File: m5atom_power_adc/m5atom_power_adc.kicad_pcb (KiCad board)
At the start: 2 copper layers, 0 parts

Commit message: refactor: 回路図をフラットから階層化に移行、ブザー回路追加
- 回路図: フラット構成から階層シート構成へ移行（共通回路の共通化）
  - メインシート（1xx）: 電源・ESP32・ADC・ブザー等トップレベル
  - RelayControl サブシート: リレードライバ回路（Q×2、D×3、R×6）
  - VoltageSense サブシート: 電圧分圧回路（C×4、R×5）
  - GroveUnit サブシート: Grove 電源スイッチ回路（Q×3、D×3、R×3）
- 回路図: リファレンス番号をページ番号+xx体系に変更
- 回路図: ブザー回路追加（LS101/MLT-8530 + Q103/AO3401A ハイサイドスイッチ、GPIO34）
- HARDWARE.md: ブザー回路仕様を追記（駆動条件・部品表）
- HARDWARE.md: 赤色LED選定（XL-1608SURC-06）追記
- HARDWARE.md: 電源系統別トレース幅・ビアサイズ表を拡充
- HARDWARE.md: LM2596スイッチングノードの配線注意事項を追記

Co-Authored-By: Claude Sonnet 4.6 <noreply@anthropic.com>
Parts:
- added C101: 220uF, Capacitor_SMD:CP_Elec_10x10, F.Cu at (33.8, 158.8)
- added C102: 220uF, Capacitor_SMD:CP_Elec_10x10, F.Cu at (56.6, 144.9)
- added C103: 10uF, Capacitor_SMD:C_0805_2012Metric, F.Cu at (116.4, 105.7)
- added C104: 1uF X7R, Capacitor_SMD:C_0603_1608Metric, F.Cu at (126.8, 109.6)
- added C105: 10uF, Capacitor_SMD:C_0805_2012Metric, F.Cu at (116.4, 108.7)
- added C106: 100nF C0G, Capacitor_SMD:C_1206_3216Metric, F.Cu at (94.2, 108.4)
- added C107: 100nF C0G, Capacitor_SMD:C_1206_3216Metric, F.Cu at (94.2, 121.8)
- added C108: 10uF, Capacitor_SMD:C_0805_2012Metric, F.Cu at (116.4, 111.7)
- added C109: 10uF, Capacitor_SMD:C_0805_2012Metric, F.Cu at (116.4, 114.7)
- added C110: 100nF C0G, Capacitor_SMD:C_1206_3216Metric, F.Cu at (94.2, 111.7)
- added C701: 22nF C0G, Capacitor_SMD:C_0805_2012Metric, F.Cu at (230.7, 135.1)
- added C702: 22nF C0G, Capacitor_SMD:C_0805_2012Metric, F.Cu at (230.7, 129.2)
- added C703: 220nF C0G, Capacitor_SMD:C_1206_3216Metric, F.Cu at (233.0, 132.2)
- added C801: 22nF C0G, Capacitor_SMD:C_0805_2012Metric, F.Cu at (243.9, 135.4)
- added C802: 22nF C0G, Capacitor_SMD:C_0805_2012Metric, F.Cu at (238.0, 135.4)
- added C803: 220nF C0G, Capacitor_SMD:C_1206_3216Metric, F.Cu at (241.0, 133.1)
- added D101: SMAJ16A, Diode_SMD:D_SMB, F.Cu at (32.4, 148.8)
- added D102: SSL36, Diode_SMD:D_SMA, F.Cu at (36.7, 148.6)
- added D103: LESD5D5.0CT1G, Diode_SMD:D_SOD-523, F.Cu at (98.8, 112.6)
- added D104: LESD5D5.0CT1G, Diode_SMD:D_SOD-523, F.Cu at (98.8, 115.0)
- added D105: SSL36, Diode_SMD:D_SMA, F.Cu at (81.3, 118.0)
- added D106: LESD5D5.0CT1G, Diode_SMD:D_SOD-523, F.Cu at (98.8, 117.5)
- added D107: SS34, Diode_SMD:D_SMA, F.Cu at (43.1, 157.0)
- added D108: LED, LED_SMD:LED_0603_1608Metric, F.Cu at (52.3, 161.3)
- added D109: 1N4148WS, Diode_SMD:D_SOD-323, F.Cu at (120.8, 126.3)
- added D201: 1N4148WS, Diode_SMD:D_SOD-323, F.Cu at (112.3, 151.8)
- added D202: LED, LED_SMD:LED_0603_1608Metric, F.Cu at (117.8, 157.3)
- added D301: 1N4148WS, Diode_SMD:D_SOD-323, F.Cu at (128.0, 151.8)
- added D302: LED, LED_SMD:LED_0603_1608Metric, F.Cu at (133.5, 157.3)
- added D401: 1N4148WS, Diode_SMD:D_SOD-323, F.Cu at (143.7, 151.8)
- added D402: LED, LED_SMD:LED_0603_1608Metric, F.Cu at (149.2, 157.3)
- added D501: SD03, Diode_SMD:D_SOD-323, F.Cu at (250.4, 52.1)
- added D502: SD03, Diode_SMD:D_SOD-323, F.Cu at (250.4, 55.1)
- added D601: SD03, Diode_SMD:D_SOD-323, F.Cu at (257.2, 86.1)
- added D602: SD03, Diode_SMD:D_SOD-323, F.Cu at (257.2, 89.0)
- added F101: Polyfuse, Fuse:Fuse_1812_4532Metric, F.Cu at (36.7, 141.8)
- added FB101: 500mA 600Ω@100MHz, Inductor_SMD:L_0805_2012Metric, F.Cu at (99.3, 124.6)
- added J101: USB_C_Receptacle_USB2.0_16P, Connector_USB:USB_C_Receptacle_HRO_TYPE-C-31-M-12, F.Cu at (54.0, 96.5)
- added J102: Conn_01x04_Pin, Connector_PinHeader_2.54mm:PinHeader_1x04_P2.54mm_Vertical, F.Cu at (143.1, 72.3)
- added J103: SubBatt, Connector_JST:JST_XH_B2B-XH-A_1x02_P2.50mm_Vertical, F.Cu at (54.0, 65.5)
- added J104: MainBatt, Connector_JST:JST_XH_B2B-XH-A_1x02_P2.50mm_Vertical, F.Cu at (54.0, 56.2)
- added J105: I2C, Connector_JST:JST_XH_S4B-XH-SM4-TB_1x04-1MP_P2.50mm_Horizontal, F.Cu at (58.3, 122.2)
- added J106: Shunt, Connector_JST:JST_XH_B2B-XH-A_1x02_P2.50mm_Vertical, F.Cu at (150.0, 59.5)
- added J201: Relay0, Connector_JST:JST_XH_B2B-XH-A_1x02_P2.50mm_Vertical, F.Cu at (113.7, 156.8)
- added J202: R0SW, Connector_JST:JST_XH_B2B-XH-A_1x02_P2.50mm_Vertical, F.Cu at (113.7, 169.2)
- added J301: Relay0, Connector_JST:JST_XH_B2B-XH-A_1x02_P2.50mm_Vertical, F.Cu at (129.3, 156.8)
- added J302: R0SW, Connector_JST:JST_XH_B2B-XH-A_1x02_P2.50mm_Vertical, F.Cu at (129.3, 169.2)
- added J401: Relay0, Connector_JST:JST_XH_B2B-XH-A_1x02_P2.50mm_Vertical, F.Cu at (145.1, 156.8)
- added J402: R0SW, Connector_JST:JST_XH_B2B-XH-A_1x02_P2.50mm_Vertical, F.Cu at (145.1, 169.2)
- added J501: GROVE-CONNECTOR, 000_Local:HY2.0-4PWB, F.Cu at (251.2, 46.7)
- added J601: GROVE-CONNECTOR, 000_Local:HY2.0-4PWB, F.Cu at (257.9, 80.7)
- added L101: 68uH, 000_Local:PSPMAA0605H-680M-IGF, F.Cu at (54.1, 156.3)
- added LS101: MLT-8530, 000_Local:MLT-8530, F.Cu at (65.5, 105.0)
- added Q101: AO3401A, Package_TO_SOT_SMD:SOT-23, F.Cu at (111.7, 94.0)
- added Q102: MMBT2222A, Package_TO_SOT_SMD:SOT-23, F.Cu at (111.7, 98.5)
- added Q103: AO3401A, Package_TO_SOT_SMD:SOT-23, F.Cu at (111.7, 102.9)
- added Q201: MMBT2222A, Package_TO_SOT_SMD:SOT-23, F.Cu at (111.8, 161.7)
- added Q301: MMBT2222A, Package_TO_SOT_SMD:SOT-23, F.Cu at (127.5, 161.7)
- added Q401: MMBT2222A, Package_TO_SOT_SMD:SOT-23, F.Cu at (143.2, 161.7)
- added Q501: AO3401A, Package_TO_SOT_SMD:SOT-23, F.Cu at (260.1, 41.0)
- added Q502: MMBT2222A, Package_TO_SOT_SMD:SOT-23, F.Cu at (260.1, 45.4)
- added Q601: AO3401A, Package_TO_SOT_SMD:SOT-23, F.Cu at (266.9, 74.9)
- added Q602: MMBT2222A, Package_TO_SOT_SMD:SOT-23, F.Cu at (266.9, 79.4)
- added R101: 10k, Resistor_SMD:R_0402_1005Metric, F.Cu at (51.5, 151.5)
- added R102: 5.1k, Resistor_SMD:R_0603_1608Metric, F.Cu at (126.8, 112.1)
- added R103: 5.1k, Resistor_SMD:R_0603_1608Metric, F.Cu at (126.8, 114.6)
- added R104: 1k, Resistor_SMD:R_0603_1608Metric, F.Cu at (55.6, 161.3)
- added R105: 10k, Resistor_SMD:R_0402_1005Metric, F.Cu at (125.2, 71.0)
- added R106: 100k, Resistor_SMD:R_0603_1608Metric, F.Cu at (134.8, 124.6)
- added R107: 2W4.7, Resistor_SMD:R_2512_6332Metric, F.Cu at (108.7, 107.6)
- added R108: 2W4.7, Resistor_SMD:R_2512_6332Metric, F.Cu at (108.7, 112.5)
- added R109: 2W4.7, Resistor_SMD:R_2512_6332Metric, F.Cu at (108.7, 117.4)
- added R110: 10k, Resistor_SMD:R_0402_1005Metric, F.Cu at (131.0, 73.0)
- added R111: 10k, Resistor_SMD:R_0402_1005Metric, F.Cu at (131.0, 75.0)
- added R112: 10k, Resistor_SMD:R_0402_1005Metric, F.Cu at (128.1, 77.0)
- added R113: 10k, Resistor_SMD:R_0402_1005Metric, F.Cu at (125.2, 75.0)
- added R114: 10k, Resistor_SMD:R_0402_1005Metric, F.Cu at (125.2, 77.0)
- added R201: 100k, Resistor_SMD:R_0603_1608Metric, F.Cu at (114.0, 173.1)
- added R202: 27k, Resistor_SMD:R_0603_1608Metric, F.Cu at (110.9, 173.1)
- added R203: 1k, Resistor_SMD:R_0603_1608Metric, F.Cu at (116.2, 151.6)
- added R204: 1k, Resistor_SMD:R_0603_1608Metric, F.Cu at (117.8, 154.2)
- added R205: 1k, Resistor_SMD:R_0603_1608Metric, F.Cu at (108.9, 162.1)
- added R301: 100k, Resistor_SMD:R_0603_1608Metric, F.Cu at (129.7, 173.1)
- added R302: 27k, Resistor_SMD:R_0603_1608Metric, F.Cu at (126.6, 173.1)
- added R303: 1k, Resistor_SMD:R_0603_1608Metric, F.Cu at (131.9, 151.6)
- added R304: 1k, Resistor_SMD:R_0603_1608Metric, F.Cu at (133.5, 154.2)
- added R305: 1k, Resistor_SMD:R_0603_1608Metric, F.Cu at (124.6, 162.1)
- added R401: 100k, Resistor_SMD:R_0603_1608Metric, F.Cu at (145.4, 173.1)
- added R402: 27k, Resistor_SMD:R_0603_1608Metric, F.Cu at (142.3, 173.1)
- added R403: 1k, Resistor_SMD:R_0603_1608Metric, F.Cu at (147.6, 151.6)
- added R404: 1k, Resistor_SMD:R_0603_1608Metric, F.Cu at (149.2, 154.2)
- added R405: 1k, Resistor_SMD:R_0603_1608Metric, F.Cu at (140.3, 162.1)
- added R501: 100k, Resistor_SMD:R_0603_1608Metric, F.Cu at (254.5, 51.9)
- added R502: 10k, Resistor_SMD:R_0402_1005Metric, F.Cu at (254.0, 54.1)
- added R601: 100k, Resistor_SMD:R_0603_1608Metric, F.Cu at (261.3, 85.8)
- added R602: 10k, Resistor_SMD:R_0402_1005Metric, F.Cu at (260.7, 88.1)
- added R701: 680k, Resistor_SMD:R_0603_1608Metric, F.Cu at (228.8, 130.8)
- added R702: 22k, Resistor_SMD:R_0402_1005Metric, F.Cu at (229.1, 133.4)
- added R703: 100, Resistor_SMD:R_0402_1005Metric, F.Cu at (230.8, 131.6)
- added R704: 100, Resistor_SMD:R_0402_1005Metric, F.Cu at (230.8, 132.8)
- added R801: 680k, Resistor_SMD:R_0603_1608Metric, F.Cu at (239.6, 137.3)
- added R802: 22k, Resistor_SMD:R_0402_1005Metric, F.Cu at (242.2, 137.0)
- added R803: 100, Resistor_SMD:R_0402_1005Metric, F.Cu at (240.4, 135.3)
- added R804: 100, Resistor_SMD:R_0402_1005Metric, F.Cu at (241.6, 135.3)
- added SW101: Boot, Button_Switch_SMD:SW_SPST_PTS810, F.Cu at (150.1, 110.7)
- added SW102: Reset, Button_Switch_SMD:SW_SPST_PTS810, F.Cu at (150.1, 115.4)
- added SW103: ~, Button_Switch_SMD:SW_SPST_PTS810, F.Cu at (150.1, 120.2)
- added SW104: ~, Button_Switch_SMD:SW_SPST_PTS810, F.Cu at (150.1, 124.9)
- added TP101: TestPoint, TestPoint:TestPoint_Pad_D1.5mm, F.Cu at (115.9, 84.7)
- added TP102: TestPoint, TestPoint:TestPoint_Pad_D1.5mm, F.Cu at (119.5, 91.8)
- added TP103: TestPoint, TestPoint:TestPoint_Pad_D1.5mm, F.Cu at (115.9, 88.2)
- added TP104: TestPoint, TestPoint:TestPoint_Pad_D1.5mm, F.Cu at (123.0, 98.9)
- added TP105: TestPoint, TestPoint:TestPoint_Pad_D1.5mm, F.Cu at (123.0, 102.4)
- added TP106: TestPoint, TestPoint:TestPoint_Pad_D1.5mm, F.Cu at (115.9, 102.4)
- added TP107: TestPoint, TestPoint:TestPoint_Pad_D1.5mm, F.Cu at (115.9, 91.8)
- added TP108: TestPoint, TestPoint:TestPoint_Pad_D1.5mm, F.Cu at (115.9, 98.9)
- added TP109: TestPoint, TestPoint:TestPoint_Pad_D1.5mm, F.Cu at (115.9, 95.3)
- added TP201: TestPoint, TestPoint:TestPoint_Pad_D1.5mm, F.Cu at (116.4, 161.4)
- added TP301: TestPoint, TestPoint:TestPoint_Pad_D1.5mm, F.Cu at (132.1, 161.4)
- added TP401: TestPoint, TestPoint:TestPoint_Pad_D1.5mm, F.Cu at (147.8, 161.4)
- added TP501: TestPoint, TestPoint:TestPoint_Pad_D1.5mm, F.Cu at (246.5, 52.4)
- added TP502: TestPoint, TestPoint:TestPoint_Pad_D1.5mm, F.Cu at (246.5, 56.0)
- added TP601: TestPoint, TestPoint:TestPoint_Pad_D1.5mm, F.Cu at (253.2, 86.4)
- added TP602: TestPoint, TestPoint:TestPoint_Pad_D1.5mm, F.Cu at (253.2, 89.9)
- added TP701: TestPoint, TestPoint:TestPoint_Pad_D1.5mm, F.Cu at (228.4, 127.9)
- added TP801: TestPoint, TestPoint:TestPoint_Pad_D1.5mm, F.Cu at (236.7, 137.7)
- added U101: LM2596S-5, Package_TO_SOT_SMD:TO-263-5_TabPin3, F.Cu at (44.7, 142.1)
- added U102: AMS1117-3.3, Package_TO_SOT_SMD:SOT-223-3_TabPin2, F.Cu at (83.0, 68.0)
- added U103: ESP32-S3-MINI-1, RF_Module:ESP32-S2-MINI-1, F.Cu at (105.5, 46.8)
- added U104: AMS1117-3.3, Package_TO_SOT_SMD:SOT-223-3_TabPin2, F.Cu at (174.3, 94.5)
- added U105: LTC2944, Package_DFN_QFN:DFN-8-1EP_3x3mm_P0.5mm_EP1.65x2.38mm, F.Cu at (174.1, 122.8)
- added U106: ADS1115IDGS, Package_SO:TSSOP-10_3x3mm_P0.5mm, F.Cu at (237.2, 130.0)
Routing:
- net +12V: track 0.00 -> 40.8 mm
- net GND1: track 0.00 -> 35.8 mm, vias 0 -> 14
- net GND2: track 0.00 -> 34.8 mm
- net Net-(D301-A): track 0.00 -> 32.6 mm
- net Net-(D201-A): track 0.00 -> 32.6 mm
- net Net-(D401-A): track 0.00 -> 32.6 mm
- net +5V: track 0.00 -> 25.4 mm
- net Net-(D107-K): track 0.00 -> 13.9 mm
- net /Relay2: track 0.00 -> 13.0 mm
- net /Relay1: track 0.00 -> 13.0 mm
- net /Relay0: track 0.00 -> 13.0 mm
- net /AIN2: track 0.00 -> 9.40 mm
- net /AIN0: track 0.00 -> 9.09 mm
- net /AIN3: track 0.00 -> 8.41 mm
- net /AIN1: track 0.00 -> 7.20 mm
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- added copper zone on B.Cu, net GND1

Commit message: fix: PCBレイアウトに合わせて回路図・PCBを微修正
Co-Authored-By: Claude Sonnet 4.6 <noreply@anthropic.com>
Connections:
- U103 pad 15: /Relay1 -> /RelaySense0
- U103 pad 16: /Relay2 -> /Relay1
- U103 pad 17: /RelaySense0 -> /RelaySense1
- U103 pad 18: /RelaySense1 -> /Relay2

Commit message: feat: PCBレイアウト完成・ドキュメントにサブシート構成を反映
- m5atom_power_adc: PCBレイアウト完成（80×82.5mm、131部品、ルーティング完了）
- GroveUnit/RelayControl サブシート更新
- CONTEXT.md/README.md: m5atom_power_adc のファイル構成にサブシート3枚・Library.pretty を追記

Co-Authored-By: Claude Sonnet 4.6 <noreply@anthropic.com>
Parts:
- removed R108, R109: 2W4.7, Resistor_SMD:R_2512_6332Metric
- removed TP106, TP108: TestPoint, TestPoint:TestPoint_Pad_D1.5mm
- added NT101: NetTie_2, NetTie:NetTie-2_SMD_Pad2.0mm, B.Cu at (74.8, 46.7)
- added NT102: NetTie_3_Tee, NetTie:NetTie-3_SMD_Pad2.0mm, B.Cu at (73.5, 90.0)
- added NT104: NetTie_2, NetTie:NetTie-2_SMD_Pad0.5mm, B.Cu at (119.0, 97.0)
- J301: value Relay0 -> Relay1
- J302: value R0SW -> R1SW
- J401: value Relay0 -> Relay2
- J402: value R0SW -> R2SW
- R107: value 2W4.7 -> 3W4.7
- SW103: value ~ -> Btn0
- SW104: value ~ -> Btn1
- moved Q601 196.8 mm to (72.3, 104.2), turned to -90 degrees
- moved D601 194.6 mm to (63.8, 107.8), turned to 180 degrees
- moved Q602 192.5 mm to (75.7, 102.1), turned to -90 degrees
- moved J601 191.5 mm to (69.4, 113.9)
- moved R601 189.6 mm to (72.3, 101.4)
- moved D602 188.2 mm to (69.6, 104.3), turned to 90 degrees
- moved R602 184.4 mm to (76.6, 99.1), turned to -90 degrees
- moved Q501 183.6 mm to (87.8, 104.2), turned to -90 degrees
- moved D501 180.0 mm to (79.3, 107.8), turned to 180 degrees
- moved J501 179.4 mm to (84.9, 113.9)
- moved TP601 178.8 mm to (75.8, 108.1)
- moved Q502 178.2 mm to (91.2, 102.1), turned to -90 degrees
- moved TP602 178.1 mm to (75.8, 105.4)
- moved R501 173.9 mm to (87.8, 101.4)
- moved D502 172.5 mm to (85.1, 104.3), turned to 90 degrees
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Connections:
- D501 pad 2: GND2 -> GND1
- D502 pad 2: GND2 -> GND1
- D601 pad 2: GND2 -> GND1
- D602 pad 2: GND2 -> GND1
- J102 pad 3: TXD0 -> RXD0
- J102 pad 4: RXD0 -> TXD0
- J103 pad 2: /BATT0_P -> +BATT
- J105 pad 1: GND2 -> GND1
- J202 pad 2: GND2 -> GND1
- J302 pad 2: GND2 -> GND1
- J402 pad 2: GND2 -> GND1
- J501 pad 4: GND2 -> GND1
- J601 pad 4: GND2 -> GND1
- Q102 pad 2: GND2 -> GND1
- Q201 pad 2: GND2 -> GND1
- Q301 pad 2: GND2 -> GND1
- Q401 pad 2: GND2 -> GND1
- Q502 pad 2: GND2 -> GND1
- Q602 pad 2: GND2 -> GND1
- R202 pad 2: GND2 -> GND1
- R302 pad 2: GND2 -> GND1
- R402 pad 2: GND2 -> GND1
- R701 pad 1: /BATT0_P -> /BATT1_P
- R702 pad 2: /BATT0_N -> /BATT1_N
- R704 pad 1: /BATT0_N -> /BATT1_N
- R801 pad 1: /BATT1_P -> +BATT
- R802 pad 2: /BATT1_N -> /BATT0_N
- R804 pad 1: /BATT1_N -> /BATT0_N
- U103 pad 10: /LTE_RX -> /LTE_EN
- U103 pad 14: /Relay0 -> /RelaySense0
- U103 pad 15: /RelaySense0 -> /Relay0
- U103 pad 16: /Relay1 -> /RelaySense1
- U103 pad 17: /RelaySense1 -> /Relay1
- U103 pad 18: /Relay2 -> /RelaySense2
- U103 pad 19: /RelaySense2 -> /Relay2
- U103 pad 20: /GU_EN -> /GU_0
- U103 pad 21: /GU_0 -> /GU_1
- U103 pad 22: /GU_1 -> /GU_EN
- U103 pad 8: /LTE_EN -> /LTE_RX
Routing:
- net +5V: track 25.4 -> 177.3 mm, vias 0 -> 7
- net +3.3V: track 0.00 -> 133.1 mm, vias 0 -> 5
- net SCL: track 0.00 -> 128.6 mm, vias 0 -> 4
- net SDA: track 0.00 -> 115.8 mm, vias 0 -> 4
- net /BATT0_N: track 0.00 -> 109.4 mm, vias 0 -> 3
- net +BATT: track 0.00 -> 99.1 mm, vias 0 -> 2
- net /BATT1_P: track 0.00 -> 82.8 mm, vias 0 -> 2
- net /BATT1_N: track 0.00 -> 82.6 mm, vias 0 -> 2
- net /LTE_RX: track 0.00 -> 80.3 mm
- net /LTE_TX: track 0.00 -> 78.3 mm
- net VBUS: track 3.37 -> 78.9 mm, vias 0 -> 2
- net /GU_0: track 0.00 -> 67.6 mm, vias 0 -> 2
- net GND2: track 34.8 -> 101.6 mm, vias 0 -> 23
- net /GU_1: track 0.00 -> 66.7 mm, vias 0 -> 2
- net ADC_RDY: track 0.00 -> 64.4 mm, vias 0 -> 2
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- added copper zone on B.Cu, net GND2
- added copper zone on B.Cu, net GNDA
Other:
- board outline added: 80 x 82.5 mm

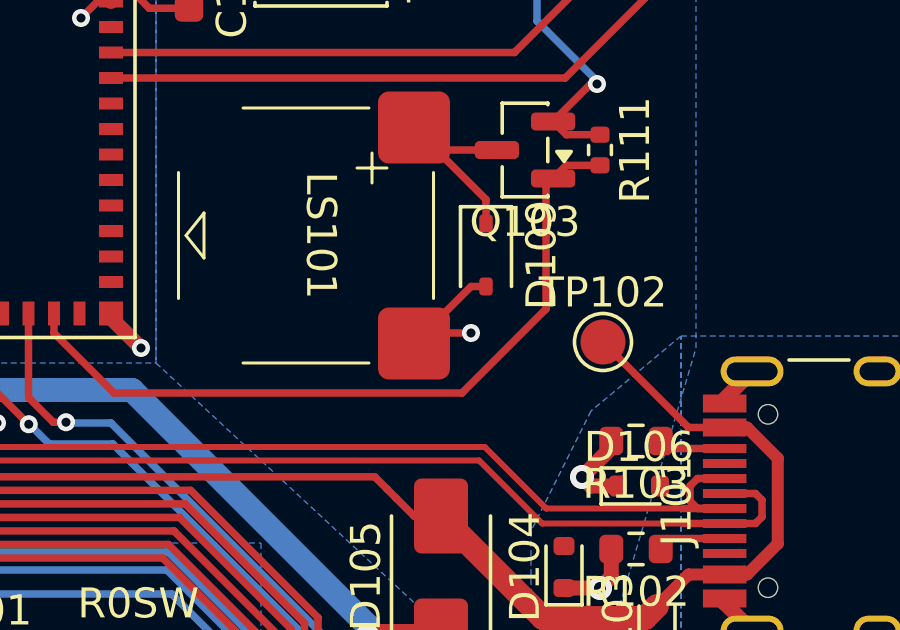
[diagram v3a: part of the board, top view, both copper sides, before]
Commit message: fix: MLT-8530直下のベタGNDを除外（うず電流対策）
フットプリントにkeeputゾーンを追加し、PCBのベタ銅をLS101 courtyard範囲から除外。

Co-Authored-By: Claude Sonnet 4.6 <noreply@anthropic.com>
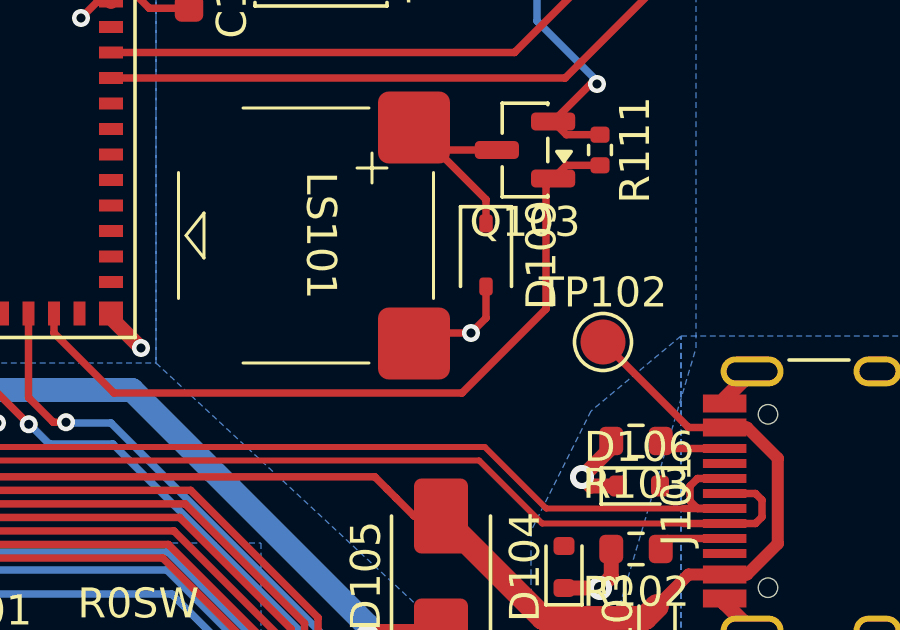
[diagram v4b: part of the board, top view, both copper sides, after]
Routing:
- net GND2: track 101.6 -> 100.2 mm

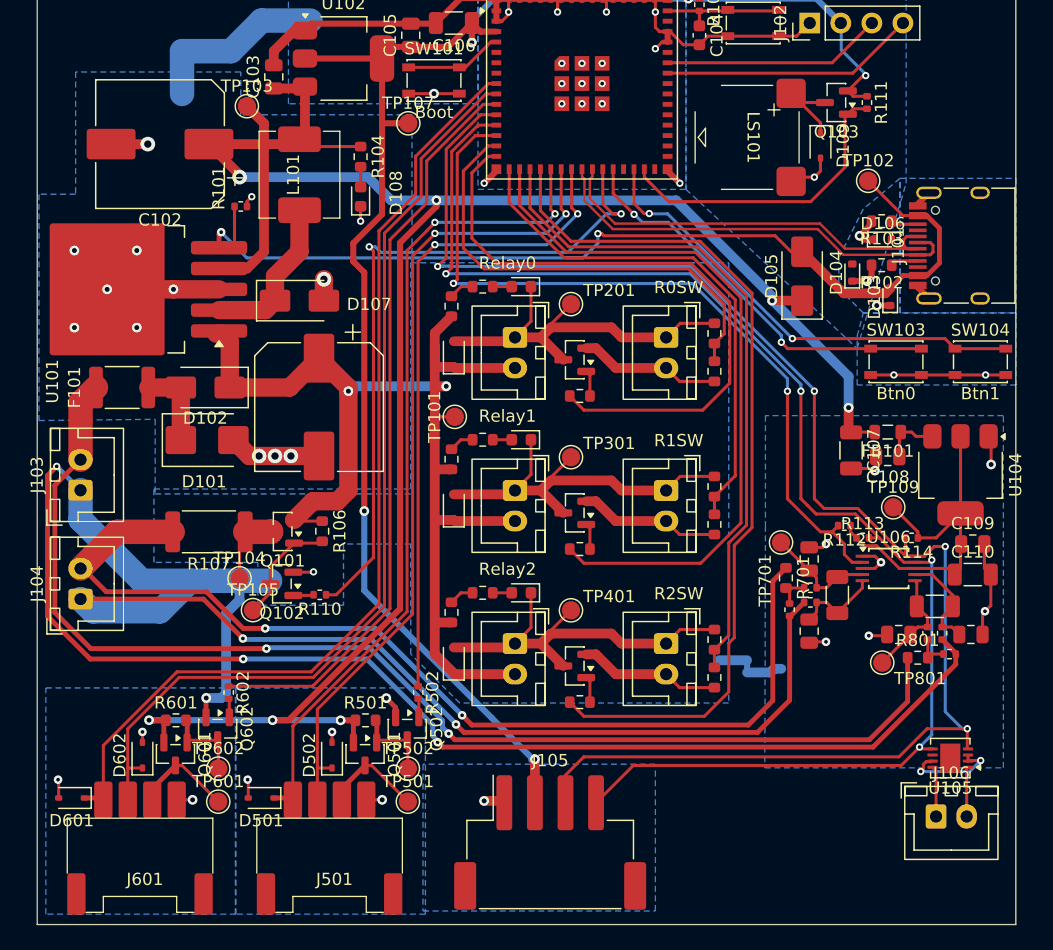
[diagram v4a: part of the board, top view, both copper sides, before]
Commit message: chore: PCBレイアウト・回路図の細部修正
- GNDプレーン追加・整理（表裏、スターグラウンド構成）
- サーマルビア追加（ESP32、LM2596）
- 孤立GND島の除去
- 各種配線修正

Co-Authored-By: Claude Sonnet 4.6 <noreply@anthropic.com>
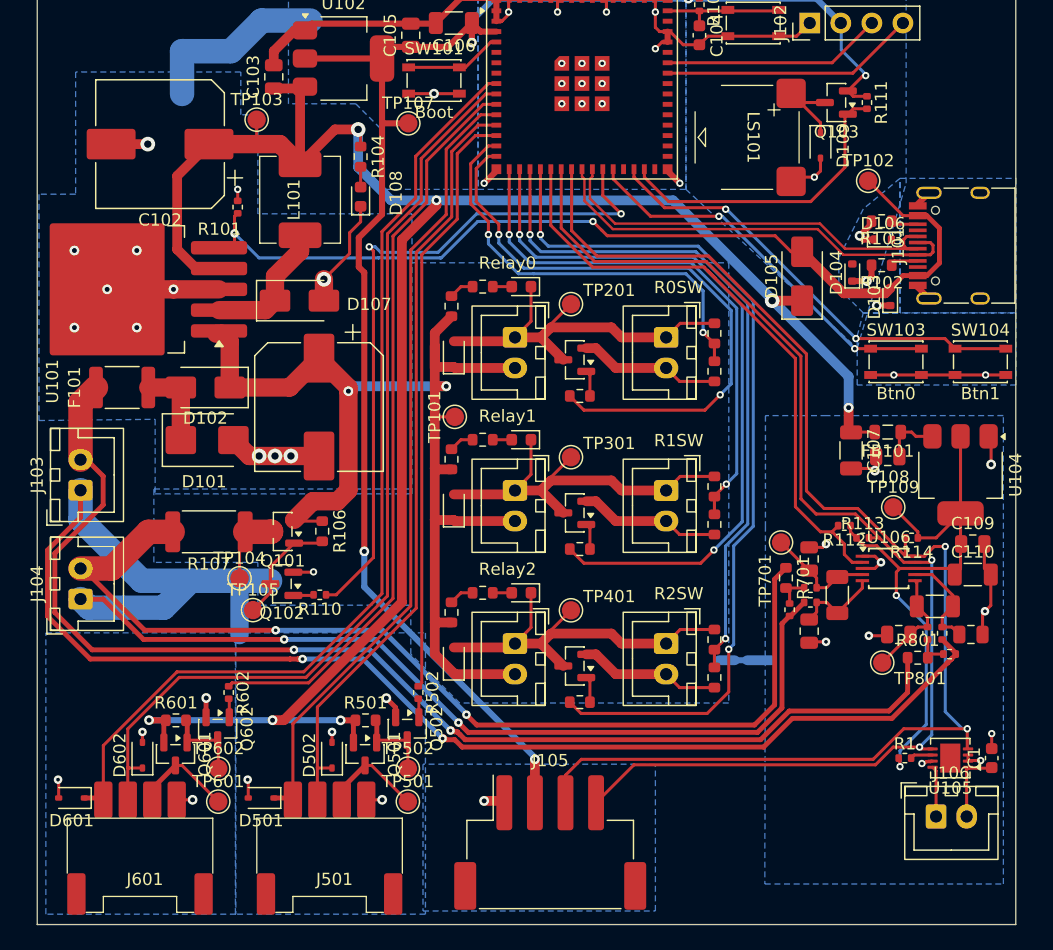
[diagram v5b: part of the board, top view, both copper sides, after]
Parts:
- added C1: 1uF X7R, Capacitor_SMD:C_0603_1608Metric, F.Cu at (139.0, 104.5)
- added R1: 10k, Resistor_SMD:R_0402_1005Metric, F.Cu at (131.9, 104.5)
- moved L101 2.05 mm to (82.5, 58.9)
- moved TP103 1.36 mm to (78.9, 52.3)
- moved NT104 0.71 mm to (118.5, 96.5), turned to 0 degrees
- moved R101 0.25 mm to (77.3, 59.5), turned to 90 degrees
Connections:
- J105 pad 3: SCL -> /SCL
- J105 pad 4: SDA -> /SDA
- R112 pad 2: ADC_RDY -> /ADC_READY
- R113 pad 2: SDA -> /SDA
- R114 pad 2: SCL -> /SCL
- U103 pad 11: SCL -> /GU_0
- U103 pad 12: SDA -> /GU_1
- U103 pad 13: ADC_RDY -> /GU_EN
- U103 pad 20: /GU_0 -> /ADC_READY
- U103 pad 21: /GU_1 -> /SDA
- U103 pad 22: /GU_EN -> /SCL
- U105 pad 4: SCL -> /SCL
- U105 pad 5: SDA -> /SDA
- U105 pad 6: unconnected-(U105-~ALCC-Pad6) -> Net-(U105-~ALCC)
- U106 pad 10: SCL -> /SCL
- U106 pad 2: ADC_RDY -> /ADC_READY
- U106 pad 9: SDA -> /SDA
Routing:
- net SCL: track 128.6 -> 0.00 mm, vias 4 -> 0
- net SDA: track 115.8 -> 0.00 mm, vias 4 -> 0
- net /SCL: track 0.00 -> 110.0 mm, vias 0 -> 2
- net /SDA: track 0.00 -> 99.4 mm, vias 0 -> 2
- net ADC_RDY: track 64.4 -> 0.00 mm, vias 2 -> 0
- net /ADC_READY: track 0.00 -> 50.7 mm
- net +3.3VA: track 29.6 -> 48.6 mm, vias 0 -> 2
- net +5V: track 177.3 -> 170.7 mm
- net GNDA: track 32.7 -> 27.2 mm, vias 9 -> 10
- net /BATT0_N: track 109.4 -> 104.5 mm, vias 3 -> 2
- net /GU_EN: track 53.3 -> 48.7 mm, vias 2 -> 0
- net /GU_1: track 66.7 -> 63.3 mm, vias 2 -> 0
- net /RelaySense0: track 38.1 -> 35.1 mm, vias 0 -> 2
- net VBUS: track 78.9 -> 76.5 mm
- net /GU_0: track 67.6 -> 65.3 mm, vias 2 -> 0
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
